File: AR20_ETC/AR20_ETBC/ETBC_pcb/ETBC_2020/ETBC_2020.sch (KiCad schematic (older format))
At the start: 28 parts, among them IC1 MC33931EK, J1 Conn_02x09_Top_Bottom, U1 ACM_2020

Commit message: ETC PCB Layout
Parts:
- added D6: Red, Capacitor_SMD:C_1206_3216Metric_Pad1.42x1.75mm_HandSolder, symbol Device:LED_Small
- added Q1: NDS356AP, Package_TO_SOT_SMD:SOT-23, symbol Device:Q_PJFET_GSD
- added R8: 1K, Resistor_SMD:R_0603_1608Metric_Pad1.05x0.95mm_HandSolder, symbol Device:R_Small
- C1, C2: Description (none) -> TPS1 and TPS2 Filtering capacitors
- C3, C9: Description (none) -> Input Capacitor Electrolytic
- D1: value DIODE -> DCBU0340-HF; footprint (none) -> Capacitor_SMD:C_0603_1608Metric_Pad1.05x0.95mm_HandSolder
- D2: footprint (none) -> Capacitor_SMD:C_1206_3216Metric_Pad1.42x1.75mm_HandSolder; Description (none) -> Green LED
- D3, D5: value D_Zener -> RB521VM-40TE-17; footprint (none) -> Diode_SMD:D_SOD-323F; Description (none) -> Zener diode for LED
- D4: footprint (none) -> Capacitor_SMD:C_1206_3216Metric_Pad1.42x1.75mm_HandSolder; Description (none) -> Yellow LED
- IC1: footprint SOP65P1030X245-33N -> ETBC_2020:SOP65P1030X245-33N; Description Motor / Motion / Ignition Controllers & Drivers 5A H-BRIDGE -> Motor Driver/Controller, DC Brush
- R3, R4: value R_Small -> 4.7K
- R6, R7: value 10K -> 1K
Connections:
- net +5V: now also R8.2
- net CANH: now also J1.17 (Pin_17)
- net CANL: now also J1.18 (Pin_18)
- net GND: now also J1.10 (Pin_10), J1.11 (Pin_11), Q1.2 (S)
- net OUT2: now also J1.5 (Pin_5), J1.6 (Pin_6); no longer J1.10 (Pin_10), J1.11 (Pin_11)
- net PWR: now also J1.3 (Pin_3), J1.4 (Pin_4)
- net SFlag: now also Q1.1 (G)
- new net: D6.1 (K), R8.1
- new net: D6.2 (A), Q1.3 (D)
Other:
- note added: "Away from critical components"
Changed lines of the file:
@@
 F 0 "IC1" H 5775 2740 50  0000 C CNN
 F 1 "MC33931EK" H 5775 2649 50  0000 C CNN
-F 2 "SOP65P1030X245-33N" H 6325 2575 50  0001 L CNN
+F 2 "ETBC_2020:SOP65P1030X245-33N" H 6325 2575 50  0001 L CNN
 F 3 "http://www.mouser.com/ds/2/302/MC33931-1126556.pdf" H 6325 2475 50  0001 L CNN
-F 4 "Motor / Motion / Ignition Controllers & Drivers 5A H-BRIDGE" H 6325 2375 50  0001 L CNN "Description"
+F 4 "Motor Driver/Controller, DC Brush" H 6325 2375 50  0001 L CNN "Description"
 F 5 "2.45" H 6325 2275 50  0001 L CNN "Height"
 F 6 "Nexperia" H 6325 2175 50  0001 L CNN "Manufacturer_Name"
@@
 F 8 "841-MC33931EK" H 6325 1975 50  0001 L CNN "Mouser Part Number"
 F 9 "https://www.mouser.com/Search/Refine.aspx?Keyword=841-MC33931EK" H 6325 1875 50  0001 L CNN "Mouser Price/Stock"
-F 10 "" H 6325 1775 50  0001 L CNN "RS Part Number"
-F 11 "" H 6325 1675 50  0001 L CNN "RS Price/Stock"
 	1    5075 2475
 	1    0    0    -1
@@
 P 5425 5350
 F 0 "D3" V 5471 5271 50  0000 R CNN
-F 1 "D_Zener" V 5380 5271 50  0000 R CNN
-F 2 "" H 5425 5350 50  0001 C CNN
-F 3 "~" H 5425 5350 50  0001 C CNN
+F 1 "RB521VM-40TE-17 " V 5400 5300 50  0000 R CNN
+F 2 "Diode_SMD:D_SOD-323F" H 5425 5350 50  0001 C CNN
+F 3 "https://no.farnell.com/rohm/rb521vm-40te-17/schottky-rect-single-40v-sod-323fl/dp/2918863" H 5425 5350 50  0001 C CNN
+F 4 "Zener diode for LED" H 5425 5350 50  0001 C CNN "Description"
 	1    5425 5350
 	0    -1   -1   0
@@
 P 4875 7150
 F 0 "D1" H 4875 7415 50  0000 C CNN
-F 1 "DIODE" H 4875 7324 50  0000 C CNN
-F 2 "" H 4875 7150 50  0001 C CNN
+F 1 "DCBU0340-HF" H 4875 7324 50  0000 C CNN
+F 2 "Capacitor_SMD:C_0603_1608Metric_Pad1.05x0.95mm_HandSolder" H 4875 7150 50  0001 C CNN
 F 3 "~" H 4875 7150 50  0001 C CNN
 	1    4875 7150
@@
 F 0 "D2" V 5471 5032 50  0000 R CNN
 F 1 "Green" V 5380 5032 50  0000 R CNN
-F 2 "" V 5425 5100 50  0001 C CNN
+F 2 "Capacitor_SMD:C_1206_3216Metric_Pad1.42x1.75mm_HandSolder" V 5425 5100 50  0001 C CNN
 F 3 "~" V 5425 5100 50  0001 C CNN
+F 4 "Green LED" H 5425 5100 50  0001 C CNN "Description"
 	1    5425 5100
 	0    -1   -1   0
@@
 P 6075 5350
 F 0 "D5" V 6121 5271 50  0000 R CNN
-F 1 "D_Zener" V 6030 5271 50  0000 R CNN
-F 2 "" H 6075 5350 50  0001 C CNN
-F 3 "~" H 6075 5350 50  0001 C CNN
+F 1 "RB521VM-40TE-17 " V 6030 5271 50  0000 R CNN
+F 2 "Diode_SMD:D_SOD-323F" H 6075 5350 50  0001 C CNN
+F 3 "https://no.farnell.com/rohm/rb521vm-40te-17/schottky-rect-single-40v-sod-323fl/dp/2918863" H 6075 5350 50  0001 C CNN
+F 4 "Zener diode for LED" H 6075 5350 50  0001 C CNN "Description"
 	1    6075 5350
 	0    -1   -1   0
@@
 F 0 "D4" V 6121 5032 50  0000 R CNN
 F 1 "Yellow" V 6030 5032 50  0000 R CNN
-F 2 "" V 6075 5100 50  0001 C CNN
+F 2 "Capacitor_SMD:C_1206_3216Metric_Pad1.42x1.75mm_HandSolder" V 6075 5100 50  0001 C CNN
 F 3 "~" V 6075 5100 50  0001 C CNN
+F 4 "Yellow LED" H 6075 5100 50  0001 C CNN "Description"
 	1    6075 5100
 	0    -1   -1   0
@@
 F 2 "Capacitor_SMD:C_0603_1608Metric_Pad1.05x0.95mm_HandSolder" H 4050 3525 50  0001 C CNN
 F 3 "~" H 4050 3525 50  0001 C CNN
+F 4 "Input Capacitor Electrolytic" H 4050 3525 50  0001 C CNN "Description"
 	1    4050 3525
 	1    0    0    -1
@@
 F 2 "Capacitor_SMD:C_0603_1608Metric_Pad1.05x0.95mm_HandSolder" H 7175 3375 50  0001 C CNN
 F 3 "~" H 7175 3375 50  0001 C CNN
+F 4 "Input Capacitor Electrolytic" H 7175 3375 50  0001 C CNN "Description"
 	1    7175 3375
 	1    0    0    -1
@@
 P 5425 5600
 F 0 "R6" H 5484 5646 50  0000 L CNN
-F 1 "10K" H 5484 5555 50  0000 L CNN
+F 1 "1K" H 5484 5555 50  0000 L CNN
 F 2 "Resistor_SMD:R_0603_1608Metric_Pad1.05x0.95mm_HandSolder" H 5425 5600 50  0001 C CNN
 F 3 "~" H 5425 5600 50  0001 C CNN
@@
 P 6075 5600
 F 0 "R7" H 6134 5646 50  0000 L CNN
-F 1 "10K" H 6134 5555 50  0000 L CNN
+F 1 "1K" H 6134 5555 50  0000 L CNN
 F 2 "Resistor_SMD:R_0603_1608Metric_Pad1.05x0.95mm_HandSolder" H 6075 5600 50  0001 C CNN
 F 3 "~" H 6075 5600 50  0001 C CNN
@@
 F 2 "Capacitor_SMD:C_0603_1608Metric_Pad1.05x0.95mm_HandSolder" H 2275 6925 50  0001 C CNN
 F 3 "~" H 2275 6925 50  0001 C CNN
+F 4 "TPS1 and TPS2 Filtering capacitors" H 2275 6925 50  0001 C CNN "Description"
 	1    2275 6925
 	1    0    0    -1
@@
 P 2750 6925
 F 0 "R4" H 2809 6971 50  0000 L CNN
-F 1 "R_Small" H 2809 6880 50  0000 L CNN
+F 1 "4.7K" H 2809 6880 50  0000 L CNN
 F 2 "Resistor_SMD:R_0603_1608Metric_Pad1.05x0.95mm_HandSolder" H 2750 6925 50  0001 C CNN
 F 3 "~" H 2750 6925 50  0001 C CNN
@@
 F 2 "Capacitor_SMD:C_0603_1608Metric_Pad1.05x0.95mm_HandSolder" H 2250 5800 50  0001 C CNN
 F 3 "~" H 2250 5800 50  0001 C CNN
+F 4 "TPS1 and TPS2 Filtering capacitors" H 2250 5800 50  0001 C CNN "Description"
 	1    2250 5800
 	1    0    0    -1
@@
 P 2725 5800
 F 0 "R3" H 2784 5846 50  0000 L CNN
-F 1 "R_Small" H 2784 5755 50  0000 L CNN
+F 1 "4.7K" H 2784 5755 50  0000 L CNN
 F 2 "Resistor_SMD:R_0603_1608Metric_Pad1.05x0.95mm_HandSolder" H 2725 5800 50  0001 C CNN
 F 3 "~" H 2725 5800 50  0001 C CNN
@@
 Text GLabel 1225 1875 0    50   Input ~ 0
 OUT1
-Text GLabel 1725 1875 2    50   Input ~ 0
+Text GLabel 1225 2375 0    50   Input ~ 0
 OUT2
 $Comp
@@
 Text GLabel 925  2800 0    50   Input ~ 0
 TPS2
-Text GLabel 2100 3200 2    50   Input ~ 0
+Text GLabel 1225 2075 0    50   Input ~ 0
 PWR
 $Comp
@@
 Text GLabel 10075 3225 2    50   Input ~ 0
 CANL
-Text GLabel 1050 3300 2    50   Input ~ 0
+Text GLabel 1725 2675 2    50   Input ~ 0
 CANL
-Text GLabel 1075 3175 2    50   Input ~ 0
-CANH
 $Comp
 L Connector_Generic:Conn_02x09_Top_Bottom J1
@@
 Text GLabel 1225 1975 0    50   Input ~ 0
 OUT1
-Text GLabel 1725 1975 2    50   Input ~ 0
+Text GLabel 1225 2275 0    50   Input ~ 0
 OUT2
 Text Notes 4275 2400 0    50   ~ 0
@@
 Text Notes 6375 4050 3    50   ~ 0
 One wide trace
-Text Notes 5975 2000 0    50   ~ 0
+Text Notes 5750 1450 0    50   ~ 0
 Need to change this and connect it directly to the MCU.\nSF can handle current up to < 0.5mA
 Wire Wire Line
 	6625 2400 6625 2475
-Wire Wire Line
-	6625 2475 6825 2475
 Connection ~ 6625 2475
-Text GLabel 6825 2475 2    50   Input ~ 0
+Text GLabel 7475 2475 2    50   Input ~ 0
 SFlag
 Text GLabel 8525 2025 0    50   Input ~ 0
 SFlag
+$Comp
+L Device:LED_Small D6
+U 1 1 5E5F07FD
+P 6925 1950
+F 0 "D6" V 6925 1900 50  0000 R CNN
+F 1 "Red" V 6825 1900 50  0000 R CNN
+F 2 "Capacitor_SMD:C_1206_3216Metric_Pad1.42x1.75mm_HandSolder" V 6925 1950 50  0001 C CNN
+F 3 "~" V 6925 1950 50  0001 C CNN
+F 4 "Yellow LED" H 6925 1950 50  0001 C CNN "Description"
+	1    6925 1950
+	0    1    1    0
+$EndComp
+$Comp
+L power:GND #PWR0108
+U 1 1 5E5F565F
+P 7675 2125
+F 0 "#PWR0108" H 7675 1875 50  0001 C CNN
+F 1 "GND" H 7680 1952 50  0000 C CNN
+F 2 "" H 7675 2125 50  0001 C CNN
+F 3 "" H 7675 2125 50  0001 C CNN
+	1    7675 2125
+	1    0    0    -1
+$EndComp
+Wire Wire Line
+	7525 2050 7675 2050
+Wire Wire Line
+	7675 2050 7675 2125
+Wire Wire Line
+	6625 2475 7325 2475
+Wire Wire Line
+	7325 2350 7325 2475
+Connection ~ 7325 2475
+Wire Wire Line
+	7325 2475 7475 2475
+Wire Wire Line
+	6925 2050 7125 2050
+$Comp
+L power:+5V #PWR0129
+U 1 1 5E60388A
+P 6925 1650
+F 0 "#PWR0129" H 6925 1500 50  0001 C CNN
+F 1 "+5V" H 6925 1800 50  0000 C CNN
+F 2 "" H 6925 1650 50  0001 C CNN
+F 3 "" H 6925 1650 50  0001 C CNN
+	1    6925 1650
+	1    0    0    -1
+$EndComp
+$Comp
+L Device:Q_PJFET_GSD Q1
+U 1 1 5E6041FA
+P 7325 2150
+F 0 "Q1" V 7653 2150 50  0000 C CNN
+F 1 "NDS356AP" V 7562 2150 50  0000 C CNN
+F 2 "Package_TO_SOT_SMD:SOT-23" H 7525 2250 50  0001 C CNN
+F 3 "http://www.farnell.com/datasheets/2286294.pdf?_ga=2.148709367.1570536622.1583238368-686461928.1578838796" H 7325 2150 50  0001 C CNN
+	1    7325 2150
+	0    -1   -1   0
+$EndComp
+$Comp
+L Device:R_Small R8
+U 1 1 5E6086AD
+P 6925 1750
+F 0 "R8" H 7025 1750 50  0000 C CNN
+F 1 "1K" H 6775 1750 50  0000 C CNN
+F 2 "Resistor_SMD:R_0603_1608Metric_Pad1.05x0.95mm_HandSolder" H 6925 1750 50  0001 C CNN
+F 3 "~" H 6925 1750 50  0001 C CNN
+	1    6925 1750
+	-1   0    0    1
+$EndComp
+Text Notes 6850 4050 1    50   ~ 0
+One wide trace
+Text Notes 4925 4100 1    50   ~ 0
+One wide trace
+Text Notes 4400 6575 0    50   ~ 0
+Away from critical components
+Text GLabel 1725 2575 2    50   Input ~ 0
+CANH
+Text GLabel 1225 2175 0    50   Input ~ 0
+PWR
+$Comp
+L power:GND #PWR0130
+U 1 1 5E630617
+P 2000 1900
+F 0 "#PWR0130" H 2000 1650 50  0001 C CNN
+F 1 "GND" H 2005 1727 50  0000 C CNN
+F 2 "" H 2000 1900 50  0001 C CNN
+F 3 "" H 2000 1900 50  0001 C CNN
+	1    2000 1900
+	1    0    0    -1
+$EndComp
+Wire Wire Line
+	1725 1975 1725 1875
+Wire Wire Line
+	1725 1875 2000 1875
+Wire Wire Line
+	2000 1875 2000 1900
+Connection ~ 1725 1875
 $EndSCHEMATC

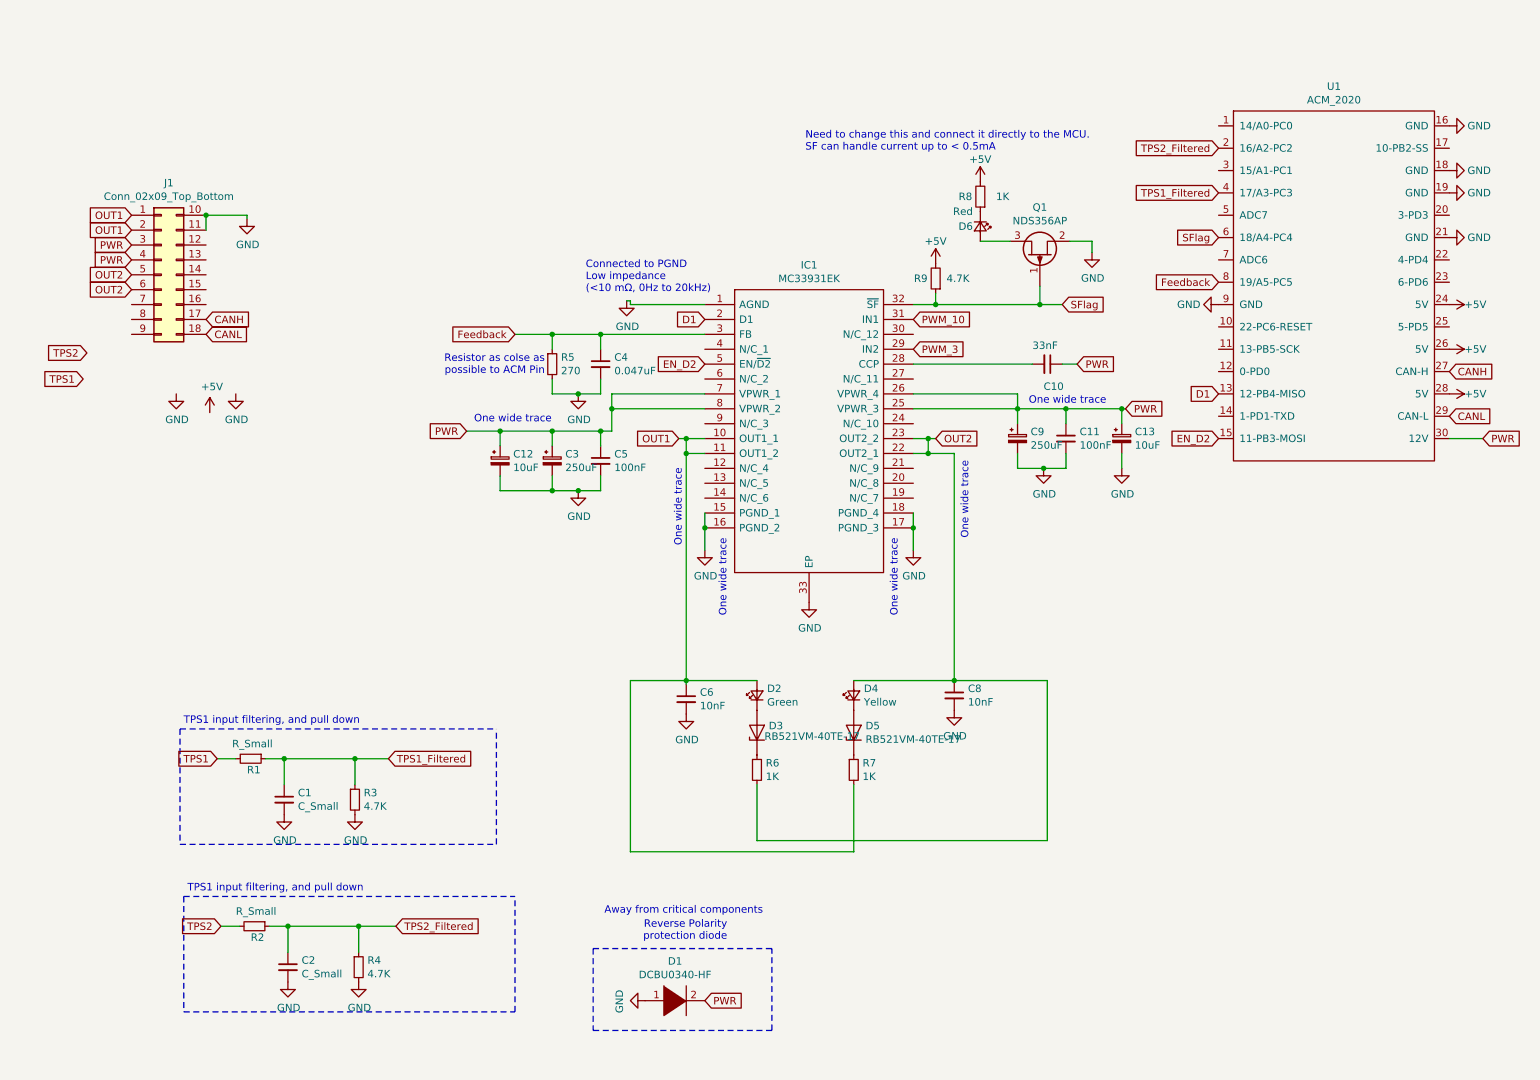
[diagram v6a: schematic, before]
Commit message: Adjusted footprints and created BOM
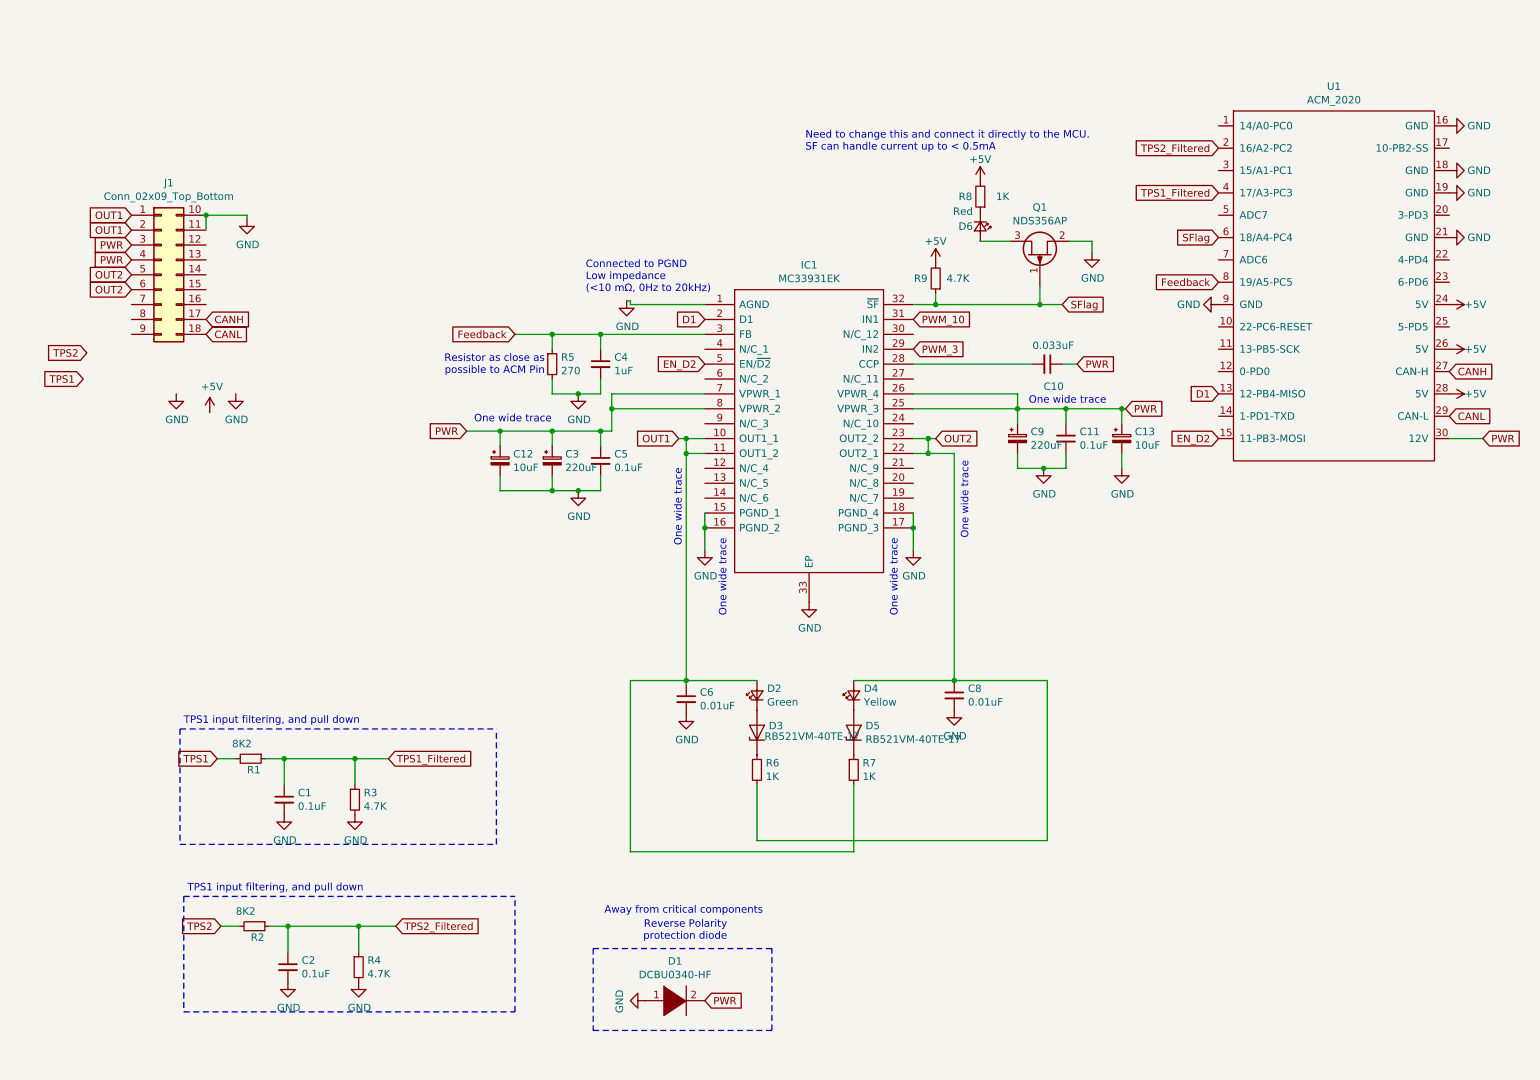
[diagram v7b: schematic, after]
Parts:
- C1, C2: value C_Small -> 0.1uF; AR-ID (none) -> AR20_ETC_012
- C10: value 33nF -> 0.033uF; AR-ID (none) -> AR20_ETC_015
- C11, C5: value 100nF -> 0.1uF; AR-ID (none) -> AR20_ETC_012
- C12, C13: footprint Capacitor_SMD:C_1206_3216Metric_Pad1.42x1.75mm_HandSolder -> Capacitor_Tantalum_SMD:CP_EIA-3216-10_Kemet-I_Pad1.58x1.35mm_HandSolder; AR-ID (none) -> AR20_ETC_016
- C3, C9: value 250uF -> 220uF; footprint Capacitor_SMD:C_0603_1608Metric_Pad1.05x0.95mm_HandSolder -> Capacitor_SMD:CP_Elec_6.3x7.7; AR-ID (none) -> AR20_ETC_013
- C4: value 0.047uF -> 1uF; AR-ID (none) -> AR20_ETC_014; Description (none) -> Feedback Capacitor
- C6, C8: value 10nF -> 0.01uF; AR-ID (none) -> AR20_ETC_017
- D1: footprint Capacitor_SMD:C_0603_1608Metric_Pad1.05x0.95mm_HandSolder -> Diode_SMD:D_1206_3216Metric_Pad1.42x1.75mm_HandSolder; AR-ID (none) -> AR20_ETC_003
- D2: footprint Capacitor_SMD:C_1206_3216Metric_Pad1.42x1.75mm_HandSolder -> Diode_SMD:D_1206_3216Metric_Pad1.42x1.75mm_HandSolder; AR-ID (none) -> AR20_ETC_005
- D3, D5: AR-ID (none) -> AR20_ETC_007
- D4: footprint Capacitor_SMD:C_1206_3216Metric_Pad1.42x1.75mm_HandSolder -> Diode_SMD:D_1206_3216Metric_Pad1.42x1.75mm_HandSolder; AR-ID (none) -> AR20_ETC_006
- D6: footprint Capacitor_SMD:C_1206_3216Metric_Pad1.42x1.75mm_HandSolder -> Diode_SMD:D_1206_3216Metric_Pad1.42x1.75mm_HandSolder; AR-ID (none) -> AR20_ETC_004
- IC1: AR-ID (none) -> AR20_ETC_001
- J1: AR-ID (none) -> AR20_ETC_002
- Q1: AR-ID (none) -> AR20_ETC_018
- R1, R2: value R_Small -> 8K2; AR-ID (none) -> AR20_ETC_011
- R3, R4, R9: AR-ID (none) -> AR20_ETC_010
- R5: AR-ID (none) -> AR20_ETC_008
- R6, R7, R8: AR-ID (none) -> AR20_ETC_009
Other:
- note added: "Resistor as close as\npossible to ACM Pin"
- note removed: "Resistor as colse as\npossible to ACM Pin"
